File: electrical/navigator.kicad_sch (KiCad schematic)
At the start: 12 parts

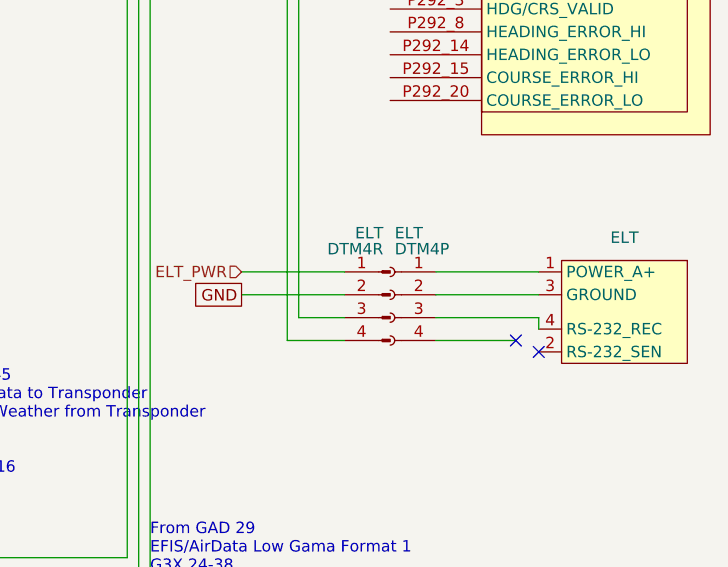
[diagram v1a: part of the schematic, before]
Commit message: Added colors for ELT
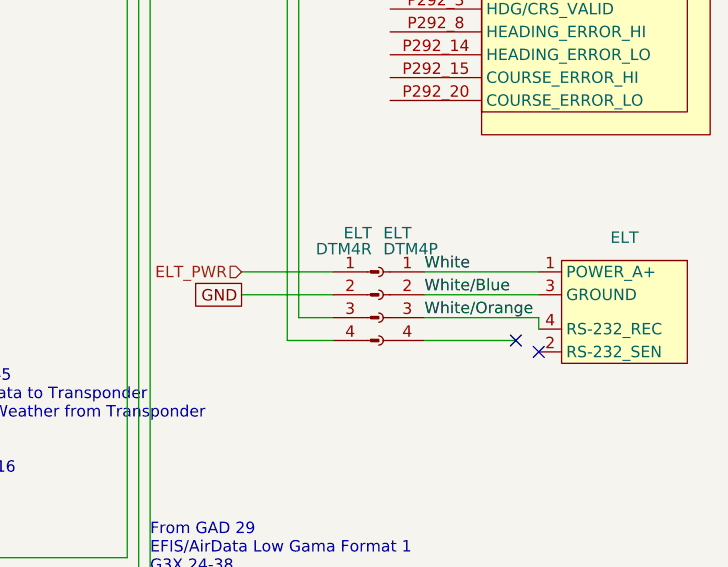
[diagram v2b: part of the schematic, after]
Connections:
- net CONNEXT_SERIAL_GND: now also ELT.1 (POWER_A+), ELT.1 (Pin_1)
- net CONNEXT_SERIAL_IN: now also ELT.2 (Pin_2), ELT.3 (GROUND)
- net CONNEXT_SERIAL_OUT: now also ELT.3 (Pin_3), ELT.4 (RS-232_REC)
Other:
- moved on the sheet: ELT
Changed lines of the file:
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@@
 	(paper "USLetter" portrait)
 	(title_block
-		(date "2025-11-19")
-		(rev "1.2.8")
+		(date "2025-12-19")
+		(rev "1.2.10")
 		(company "N78HR")
 	)
@@
 	(wire
 		(pts
-			(xy 148.59 133.35) (xy 153.67 133.35)
-		)
-		(stroke
-			(width 0)
-			(type default)
-		)
-	)
-	(wire
-		(pts
-			(xy 163.83 135.89) (xy 172.72 135.89)
+			(xy 148.59 133.35) (xy 152.4 133.35)
+		)
+		(stroke
+			(width 0)
+			(type default)
+		)
+	)
+	(wire
+		(pts
+			(xy 162.56 135.89) (xy 172.72 135.89)
 		)
 		(stroke
@@
 	(wire
 		(pts
-			(xy 142.24 130.81) (xy 153.67 130.81)
-		)
-		(stroke
-			(width 0)
-			(type default)
-		)
-	)
-	(wire
-		(pts
-			(xy 142.24 128.27) (xy 153.67 128.27)
+			(xy 142.24 130.81) (xy 152.4 130.81)
+		)
+		(stroke
+			(width 0)
+			(type default)
+		)
+	)
+	(wire
+		(pts
+			(xy 142.24 128.27) (xy 152.4 128.27)
 		)
 		(stroke
@@
 	(wire
 		(pts
-			(xy 147.32 135.89) (xy 153.67 135.89)
+			(xy 147.32 135.89) (xy 152.4 135.89)
 		)
 		(stroke
@@
 	(wire
 		(pts
-			(xy 163.83 130.81) (xy 175.26 130.81)
+			(xy 162.56 130.81) (xy 175.26 130.81)
 		)
 		(stroke
@@
 	(wire
 		(pts
-			(xy 163.83 128.27) (xy 175.26 128.27)
+			(xy 162.56 128.27) (xy 175.26 128.27)
 		)
 		(stroke
@@
 	(wire
 		(pts
-			(xy 163.83 133.35) (xy 175.26 133.35)
+			(xy 162.56 133.35) (xy 175.26 133.35)
 		)
 		(stroke
@@
 	)
 	(label "White{slash}Blue"
+		(at 162.56 130.81 0)
+		(effects
+			(font
+				(size 1.27 1.27)
+			)
+			(justify left bottom)
+		)
+	)
+	(label "White"
+		(at 162.56 128.27 0)
+		(effects
+			(font
+				(size 1.27 1.27)
+			)
+			(justify left bottom)
+		)
+	)
+	(label "White{slash}Blue"
 		(at 160.02 31.75 180)
 		(effects
@@
 			)
 			(justify right bottom)
+		)
+	)
+	(label "White{slash}Orange"
+		(at 162.56 133.35 0)
+		(effects
+			(font
+				(size 1.27 1.27)
+			)
+			(justify left bottom)
 		)
 	)
@@
 	(symbol
 		(lib_id "Connector:Conn_01x04_Socket")
-		(at 158.75 130.81 0)
+		(at 157.48 130.81 0)
 		(mirror y)
 		(unit 1)
@@
 		(dnp no)
 		(property "Reference" "ELT"
-			(at 159.258 123.952 0)
+			(at 157.988 123.952 0)
 			(effects
 				(font
@@
 		)
 		(property "Value" "DTM4P"
-			(at 159.258 125.73 0)
+			(at 157.988 125.73 0)
 			(effects
 				(font
@@
 		)
 		(property "Footprint" ""
-			(at 158.75 130.81 0)
+			(at 157.48 130.81 0)
 			(effects
 				(font
@@
 		)
 		(property "Datasheet" "~"
-			(at 158.75 130.81 0)
+			(at 157.48 130.81 0)
 			(effects
 				(font
@@
 		)
 		(property "Description" "Generic connector, single row, 01x04, script generated"
-			(at 158.75 130.81 0)
+			(at 157.48 130.81 0)
 			(effects
 				(font
@@
 	(symbol
 		(lib_id "Connector:Conn_01x04_Pin")
-		(at 158.75 130.81 0)
+		(at 157.48 130.81 0)
 		(mirror y)
 		(unit 1)
@@
 		(dnp no)
 		(property "Reference" "ELT"
-			(at 157.988 123.952 0)
+			(at 156.718 123.952 0)
 			(effects
 				(font
@@
 		)
 		(property "Value" "DTM4R"
-			(at 157.988 125.73 0)
+			(at 156.718 125.73 0)
 			(effects
 				(font
@@
 		)
 		(property "Footprint" ""
-			(at 158.75 130.81 0)
+			(at 157.48 130.81 0)
 			(effects
 				(font
@@
 		)
 		(property "Datasheet" "~"
-			(at 158.75 130.81 0)
+			(at 157.48 130.81 0)
 			(effects
 				(font
@@
 		)
 		(property "Description" "Generic connector, single row, 01x04, script generated"
-			(at 158.75 130.81 0)
-			(effects
-				(font
+			(at 157.48 130.81 0)
+			(effects
+				(font
